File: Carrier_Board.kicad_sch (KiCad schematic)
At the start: 6 parts

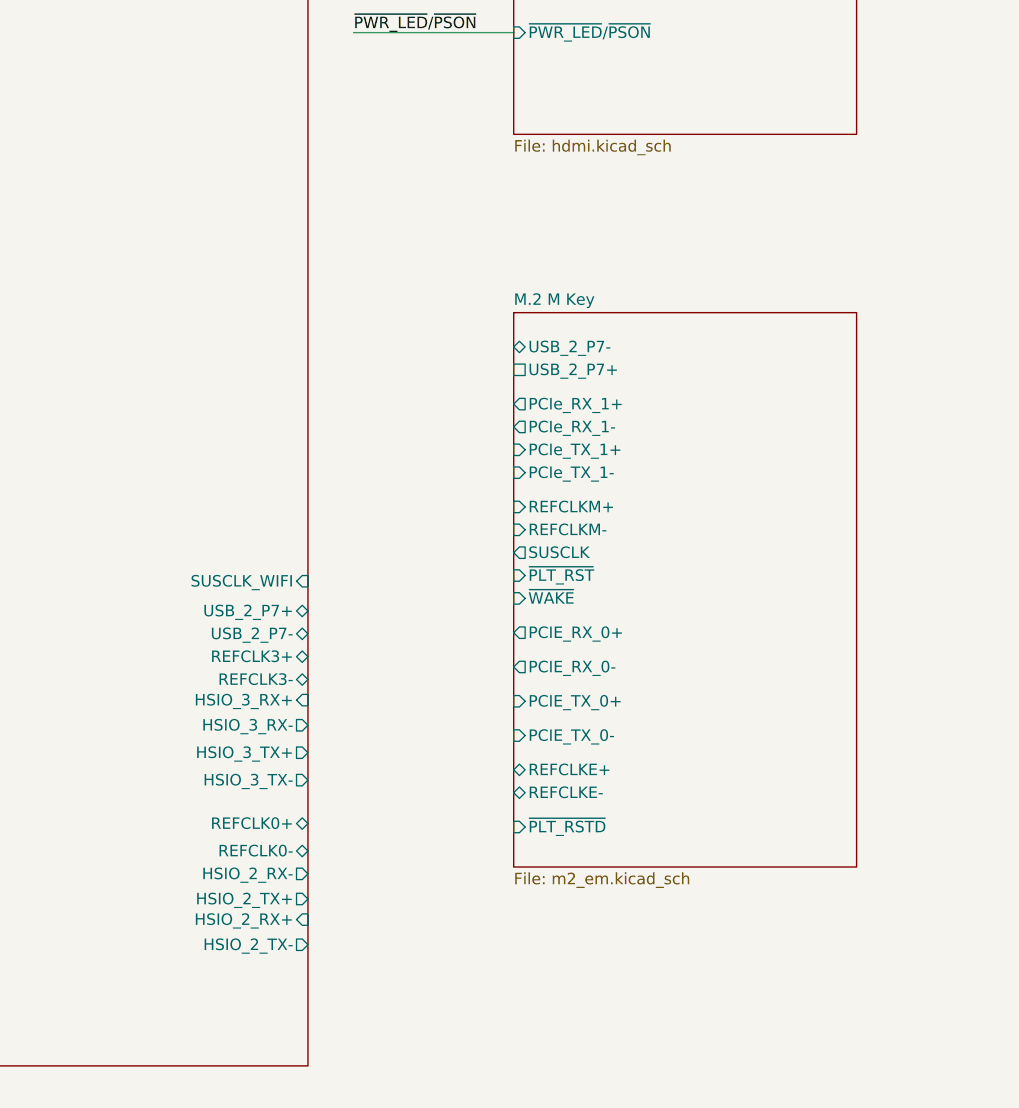
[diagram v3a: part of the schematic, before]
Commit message: finished the entire schematic capture for each of the sub sheets .and then the next part is to .fix all the erc errors when impoting the shematic in to the pcb to get readu for routing
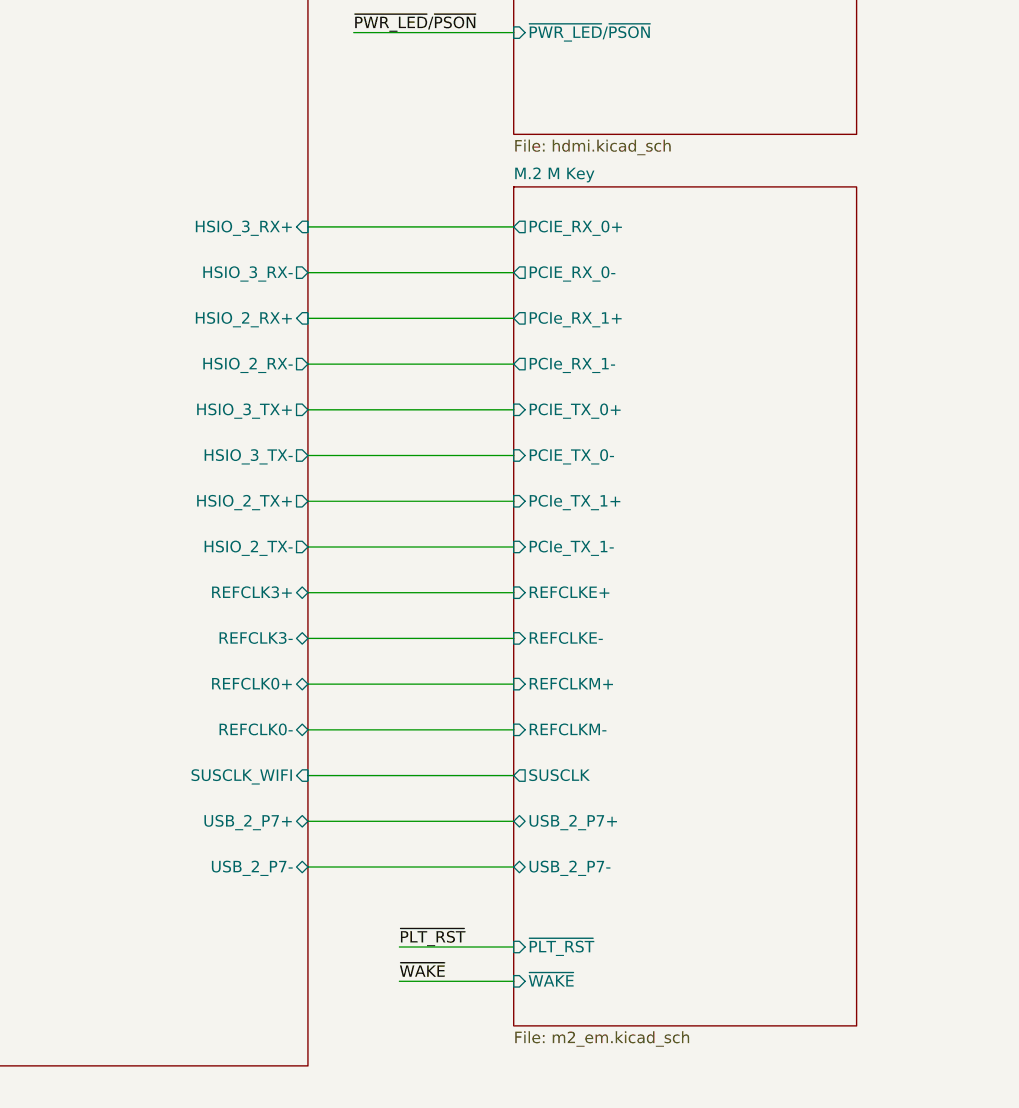
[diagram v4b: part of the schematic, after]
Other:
- sheet M.2 M Key ports: added none; removed ~{PLT_RSTD}

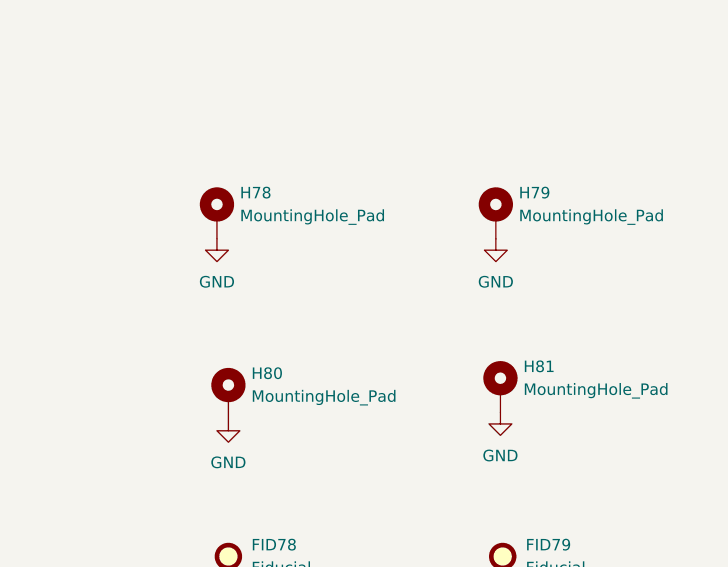
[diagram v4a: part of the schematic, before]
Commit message: Updated all the footprints into the pcb editor but all the designator numbers have changed... I have tp go back and fix each one
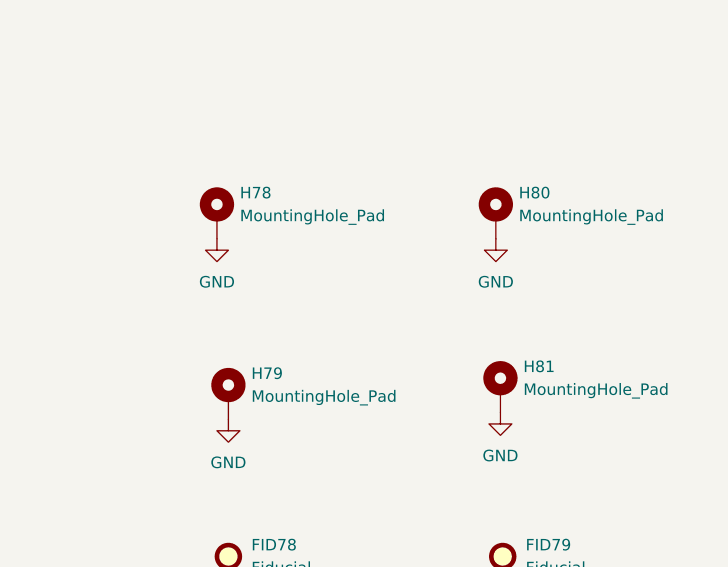
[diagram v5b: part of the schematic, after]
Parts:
- FID78, FID79: footprint (none) -> Fiducial:Fiducial_0.5mm_Mask1mm
- H78, H81: footprint (none) -> A_HDJ_Library:MountingHole_3.2mm_M3_Pad_Via
- H79: renamed from H80; footprint (none) -> A_HDJ_Library:MountingHole_3.2mm_M3_Pad_Via
- H80: renamed from H79; footprint (none) -> A_HDJ_Library:MountingHole_3.2mm_M3_Pad_Via
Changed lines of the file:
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@@
 			)
 		)
-		(property "Footprint" ""
+		(property "Footprint" "Fiducial:Fiducial_0.5mm_Mask1mm"
 			(at 441.96 345.44 0)
 			(hide yes)
@@
 		)
 		(property "Description" "Fiducial Marker"
+			(at 441.96 345.44 0)
+			(hide yes)
+			(show_name no)
+			(do_not_autoplace no)
+			(effects
+				(font
+					(size 1.27 1.27)
+				)
+			)
+		)
+		(property "KLC_S3.3" ""
+			(at 441.96 345.44 0)
+			(hide yes)
+			(show_name no)
+			(do_not_autoplace no)
+			(effects
+				(font
+					(size 1.27 1.27)
+				)
+			)
+		)
+		(property "KLC_S4.1" ""
 			(at 441.96 345.44 0)
 			(hide yes)
@@
 			)
 		)
-		(property "Footprint" ""
+		(property "Footprint" "A_HDJ_Library:MountingHole_3.2mm_M3_Pad_Via"
 			(at 472.186 326.898 0)
 			(hide yes)
@@
 		)
 		(property "Description" "Mounting Hole with connection"
+			(at 472.186 326.898 0)
+			(hide yes)
+			(show_name no)
+			(do_not_autoplace no)
+			(effects
+				(font
+					(size 1.27 1.27)
+				)
+			)
+		)
+		(property "KLC_S3.3" ""
+			(at 472.186 326.898 0)
+			(hide yes)
+			(show_name no)
+			(do_not_autoplace no)
+			(effects
+				(font
+					(size 1.27 1.27)
+				)
+			)
+		)
+		(property "KLC_S4.1" ""
 			(at 472.186 326.898 0)
 			(hide yes)
@@
 		(dnp no)
 		(fields_autoplaced yes)
-		(property "Reference" "H79"
+		(property "Reference" "H80"
 			(at 474.218 305.0539 0)
 			(show_name no)
@@
 			)
 		)
-		(property "Footprint" ""
+		(property "Footprint" "A_HDJ_Library:MountingHole_3.2mm_M3_Pad_Via"
 			(at 471.678 307.594 0)
 			(hide yes)
@@
 		)
 		(property "Description" "Mounting Hole with connection"
+			(at 471.678 307.594 0)
+			(hide yes)
+			(show_name no)
+			(do_not_autoplace no)
+			(effects
+				(font
+					(size 1.27 1.27)
+				)
+			)
+		)
+		(property "KLC_S3.3" ""
+			(at 471.678 307.594 0)
+			(hide yes)
+			(show_name no)
+			(do_not_autoplace no)
+			(effects
+				(font
+					(size 1.27 1.27)
+				)
+			)
+		)
+		(property "KLC_S4.1" ""
 			(at 471.678 307.594 0)
 			(hide yes)
@@
 			(project "Carrier_Board"
 				(path "/e768274e-12f3-4f83-96f6-abb7638e0bc1"
-					(reference "H79")
+					(reference "H80")
 					(unit 1)
 				)
@@
 			)
 		)
-		(property "Footprint" ""
+		(property "Footprint" "Fiducial:Fiducial_0.5mm_Mask1mm"
 			(at 472.44 345.44 0)
 			(hide yes)
@@
 		)
 		(property "Description" "Fiducial Marker"
+			(at 472.44 345.44 0)
+			(hide yes)
+			(show_name no)
+			(do_not_autoplace no)
+			(effects
+				(font
+					(size 1.27 1.27)
+				)
+			)
+		)
+		(property "KLC_S3.3" ""
+			(at 472.44 345.44 0)
+			(hide yes)
+			(show_name no)
+			(do_not_autoplace no)
+			(effects
+				(font
+					(size 1.27 1.27)
+				)
+			)
+		)
+		(property "KLC_S4.1" ""
 			(at 472.44 345.44 0)
 			(hide yes)
@@
 		(dnp no)
 		(fields_autoplaced yes)
-		(property "Reference" "#PWR080"
+		(property "Reference" "#PWR079"
 			(at 441.96 336.55 0)
 			(hide yes)
@@
 			(project "Carrier_Board"
 				(path "/e768274e-12f3-4f83-96f6-abb7638e0bc1"
-					(reference "#PWR080")
+					(reference "#PWR079")
 					(unit 1)
 				)
@@
 		(dnp no)
 		(fields_autoplaced yes)
-		(property "Reference" "#PWR079"
+		(property "Reference" "#PWR080"
 			(at 471.678 316.484 0)
 			(hide yes)
@@
 			(project "Carrier_Board"
 				(path "/e768274e-12f3-4f83-96f6-abb7638e0bc1"
-					(reference "#PWR079")
+					(reference "#PWR080")
 					(unit 1)
 				)
@@
 		(dnp no)
 		(fields_autoplaced yes)
-		(property "Reference" "H80"
+		(property "Reference" "H79"
 			(at 444.5 325.1199 0)
 			(show_name no)
@@
 			)
 		)
-		(property "Footprint" ""
+		(property "Footprint" "A_HDJ_Library:MountingHole_3.2mm_M3_Pad_Via"
 			(at 441.96 327.66 0)
 			(hide yes)
@@
 		)
 		(property "Description" "Mounting Hole with connection"
+			(at 441.96 327.66 0)
+			(hide yes)
+			(show_name no)
+			(do_not_autoplace no)
+			(effects
+				(font
+					(size 1.27 1.27)
+				)
+			)
+		)
+		(property "KLC_S3.3" ""
+			(at 441.96 327.66 0)
+			(hide yes)
+			(show_name no)
+			(do_not_autoplace no)
+			(effects
+				(font
+					(size 1.27 1.27)
+				)
+			)
+		)
+		(property "KLC_S4.1" ""
 			(at 441.96 327.66 0)
 			(hide yes)
@@
 			(project "Carrier_Board"
 				(path "/e768274e-12f3-4f83-96f6-abb7638e0bc1"
-					(reference "H80")
+					(reference "H79")
 					(unit 1)
 				)
@@
 			)
 		)
-		(property "Footprint" ""
+		(property "Footprint" "A_HDJ_Library:MountingHole_3.2mm_M3_Pad_Via"
 			(at 440.69 307.594 0)
 			(hide yes)
@@
 			(at 440.69 307.594 0)
 			(hide yes)
+			(show_name no)
+			(do_not_autoplace no)
+			(effects
+				(font
+					(size 1.27 1.27)
+				)
+			)
+		)
+		(property "KLC_S3.3" ""
+			(at 440.69 307.594 0)
+			(hide yes)
+			(show_name no)
+			(do_not_autoplace no)
+			(effects
+				(font
+					(size 1.27 1.27)
+				)
+			)
+		)
+		(property "KLC_S4.1" ""
+			(at 440.69 307.594 0)
+			(hide yes)
